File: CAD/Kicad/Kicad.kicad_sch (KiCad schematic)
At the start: 0 parts

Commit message: Started KiCAD work
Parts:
- added C1, C2: C, symbol Device:C
- added J1: USB_B_Mini, symbol Connector:USB_B_Mini
- added R1: 150R, symbol Device:R
- added R2: 240R, symbol Device:R
- added U1: AMS1117, Package_TO_SOT_SMD:SOT-223-3_TabPin2, symbol Regulator_Linear:AMS1117
- added U2: ESP8266EX, Package_DFN_QFN:QFN-32-1EP_5x5mm_P0.5mm_EP3.45x3.45mm, symbol MCU_Espressif:ESP8266EX
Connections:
- new net: C2.2, U2.1 (VDDA)
- new net: J1.5 (GND), R2.2, U2.33 (GND)
- new net: R1.2, R2.1, U1.1 (ADJ)
- new net: C2.1, R1.1, U1.2 (VO)
- new net: C1.1, U1.3 (VI)
- new net: C1.2, J1.1 (VBUS)
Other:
- note added: "USB Interface"

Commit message: More PCB stuff
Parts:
- added R_USB_D+, R_USB_D-: 27R, symbol Device:R
- added SW1: SW_SPST, symbol Switch:SW_SPST
- added U3: FT230XS, Package_SO:SSOP-16_3.9x4.9mm_P0.635mm, symbol Interface_USB:FT230XS
- C1, C2: value C -> 10C
- renumbered R2 to R_CNTRL_1, R1 to R_CNTRL_2
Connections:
- net at U2.25 (U0RXD): now also U3.1 (TXD)
- net at U2.26 (U0TXD): now also U3.4 (RXD)
- net GND: now reaches J1.5 (GND), R_CNTRL_1.2, U2.33 (GND)
- net GND: now also J1.SH (Shield), SW1.2 (B)
- net VCC: now reaches C2.1, R_CNTRL_2.1, U1.2 (VO)
- net VCC: now also U3.3 (VCCIO)
- net +5V: now reaches C1.2, J1.1 (VBUS)
- net at J1.2 (D-): now also R_USB_D-.1
- net at J1.3 (D+): now also R_USB_D+.2
- net at J1.4 (ID): now also SW1.1 (A)
- new net: R_USB_D-.2, U3.9 (USBDM)
- new net: U3.13 (GND), U3.5 (GND)
- new net: R_USB_D+.1, U3.8 (USBDP)
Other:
- note added: "Switch to change USB operation mode"
- moved on the sheet: C1, J1

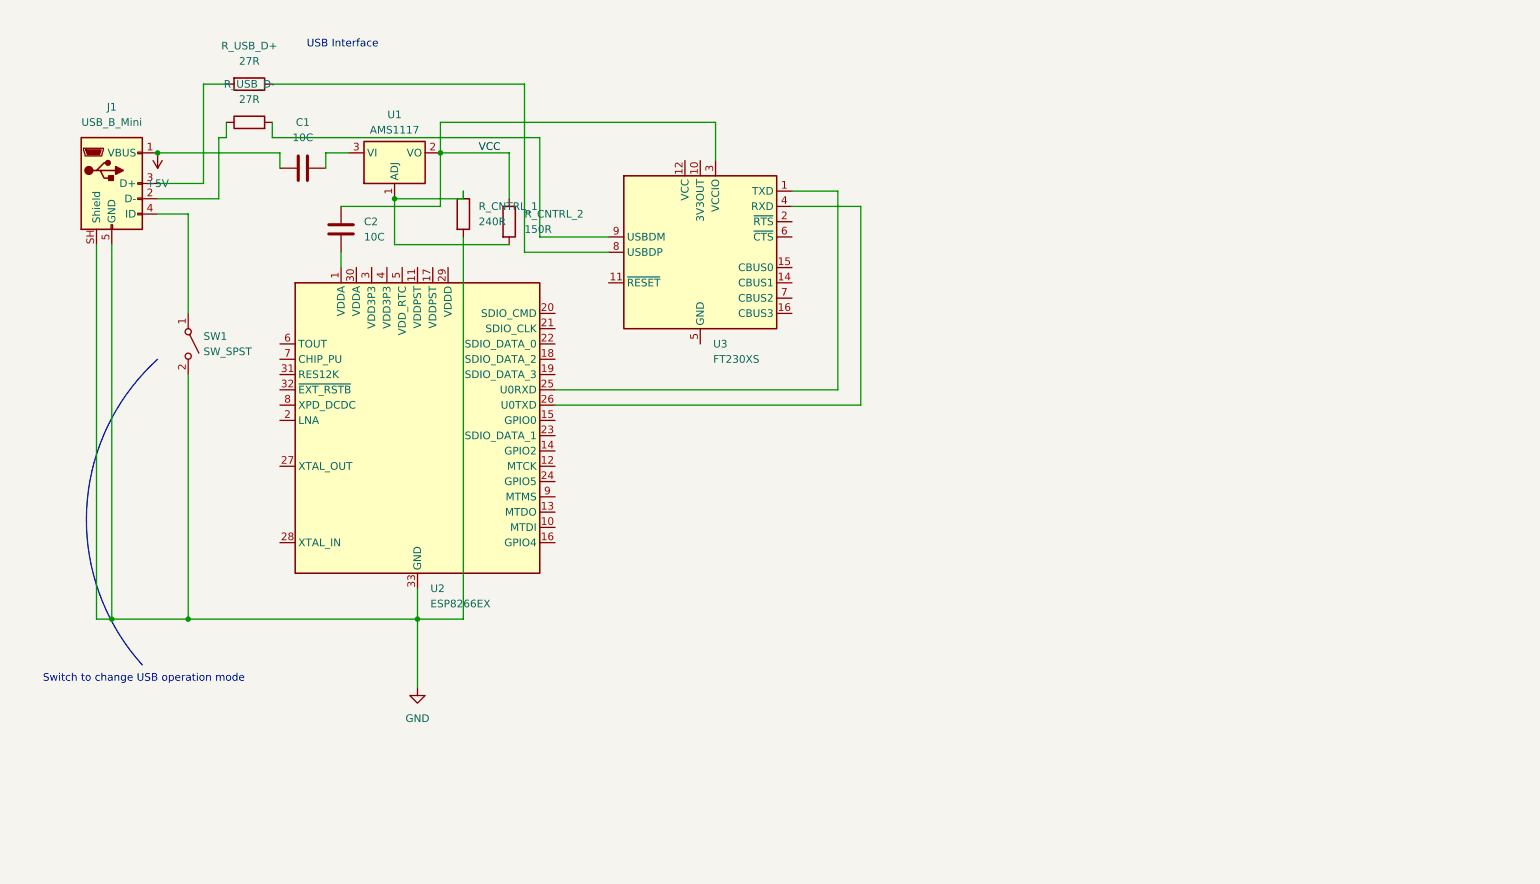
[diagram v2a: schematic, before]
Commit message: Added more and finalize basic serial connection
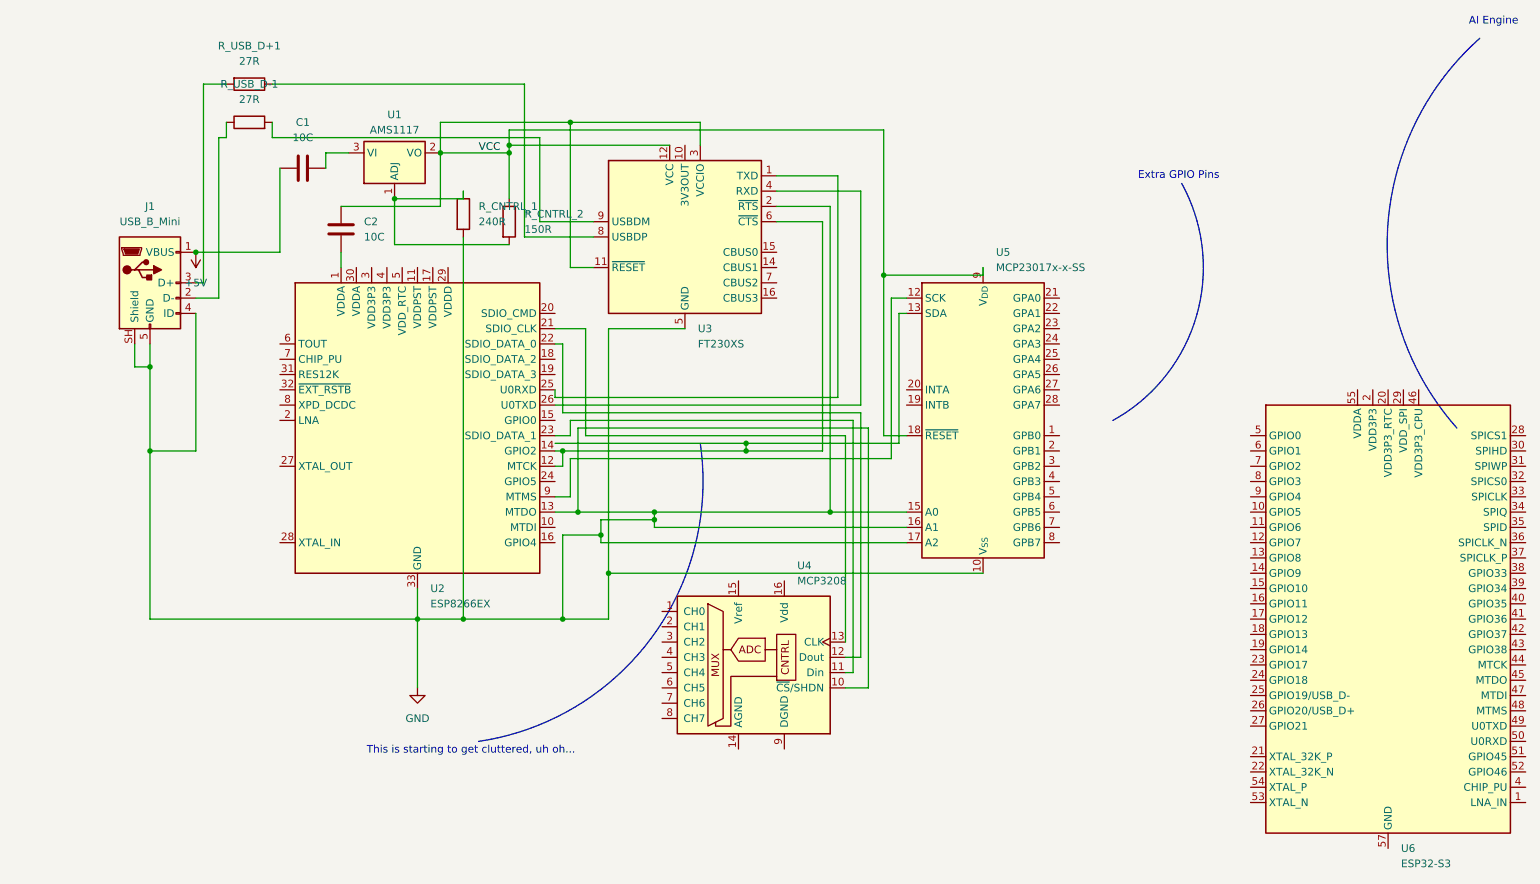
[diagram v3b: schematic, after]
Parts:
- removed SW1: SW_SPST, symbol Switch:SW_SPST
- added U4: MCP3208, symbol Analog_ADC:MCP3208
- added U5: MCP23017x-x-SS, Package_SO:SSOP-28_5.3x10.2mm_P0.65mm, symbol Interface_Expansion:MCP23017x-x-SS
- added U6: ESP32-S3, Package_DFN_QFN:QFN-56-1EP_7x7mm_P0.4mm_EP4x4mm, symbol MCU_Espressif:ESP32-S3
- renumbered R_USB_D+ to R_USB_D+1, R_USB_D- to R_USB_D-1
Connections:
- net GND: now also J1.4 (ID), U2.13 (MTDO), U3.13 (GND), U3.2 (~{RTS}), U3.5 (GND), U4.10 (~{CS}/SHDN), U5.10 (V_{SS}), U5.15 (A0), U5.16 (A1), U5.17 (A2)
- net VCC: now also U3.11 (~{RESET}), U3.12 (VCC), U5.18 (~{RESET}), U5.9 (V_{DD})
- net at U2.12 (MTCK): now also U2.14 (GPIO2), U3.6 (~{CTS}), U5.13 (SDA)
- net at U2.21 (SDIO_CLK): now also U4.13 (CLK)
- net at U2.22 (SDIO_DATA_0): now also U4.12 (Dout)
- net at U2.23 (SDIO_DATA_1): now also U4.11 (Din)
- net at U2.9 (MTMS): now also U5.12 (SCK)
- new net: U6.2 (VDD3P3), U6.3 (VDD3P3)
- new net: U6.55 (VDDA), U6.56 (VDDA)
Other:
- note added: "AI Engine"
- note added: "Extra GPIO Pins"
- note added: "This is starting to get cluttered, uh oh..."
- note removed: "Switch to change USB operation mode"
- note removed: "USB Interface"
- moved on the sheet: J1, U3

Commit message: Tweaked out and redid the entire main PCB on a Tuesday Afternoon
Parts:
- removed J1: USB_B_Mini, symbol Connector:USB_B_Mini
- removed R_CNTRL_1: 240R, symbol Device:R
- removed R_CNTRL_2: 150R, symbol Device:R
- removed R_USB_D+1, R_USB_D-1: 27R, symbol Device:R
- removed U1: AMS1117, Package_TO_SOT_SMD:SOT-223-3_TabPin2, symbol Regulator_Linear:AMS1117
- removed U2: ESP8266EX, Package_DFN_QFN:QFN-32-1EP_5x5mm_P0.5mm_EP3.45x3.45mm, symbol MCU_Espressif:ESP8266EX
- removed U3: FT230XS, Package_SO:SSOP-16_3.9x4.9mm_P0.635mm, symbol Interface_USB:FT230XS
- removed U4: MCP3208, symbol Analog_ADC:MCP3208
- removed U5: MCP23017x-x-SS, Package_SO:SSOP-28_5.3x10.2mm_P0.65mm, symbol Interface_Expansion:MCP23017x-x-SS
- removed U6: ESP32-S3, Package_DFN_QFN:QFN-56-1EP_7x7mm_P0.4mm_EP4x4mm, symbol MCU_Espressif:ESP32-S3
- added AE1: PCB_ANT, symbol Device:Antenna_Dipole
- added C10: 100nF, symbol Device:C
- added C3, C4: 0.1uF, symbol Device:C
- added C5: 1uF, symbol Device:C
- added C6, C7, C8, C9: C, symbol Device:C
- added D1, D2: LED, symbol Device:LED
- added D3: PWR_LED_1, symbol Device:LED
- added D4: PWR_LED_2, symbol Device:LED
- added FB1: FerriteBead, symbol Device:FerriteBead
- added J1: USB_C_Receptacle_USB2.0_14P, symbol Connector:USB_C_Receptacle_USB2.0_14P
- added J2: PWR_CONN, symbol Connector:Conn_01x03_Pin
- added L1: L, symbol Device:L
- added L2: 4.3nH, symbol Device:L
- added R1, R2: R, symbol Device:R
- added R_PWR_ADJ_1: 60, symbol Device:R
- added R_PWR_ADJ_2: 100, symbol Device:R
- added R_SPI_CLOCK: 200, symbol Device:R
- added U1: ESP8266EX, Package_DFN_QFN:QFN-32-1EP_5x5mm_P0.5mm_EP3.45x3.45mm, symbol MCU_Espressif:ESP8266EX
- added U2: AMS1117, Package_TO_SOT_SMD:SOT-223-3_TabPin2, symbol Regulator_Linear:AMS1117
- added U3: SST25VF080B-50-4x-S2Ax, Package_SO:SOIC-8_5.3x5.3mm_P1.27mm, symbol Memory_Flash:SST25VF080B-50-4x-S2Ax
- added U4: FT230XS, Package_SO:SSOP-16_3.9x4.9mm_P0.635mm, symbol Interface_USB:FT230XS
- added U5: ESP32-S3, Package_DFN_QFN:QFN-56-1EP_7x7mm_P0.4mm_EP4x4mm, symbol MCU_Espressif:ESP32-S3
- added Y1: Crystal_GND24, symbol Device:Crystal_GND24
- C1, C2: value 10C -> C
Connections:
- net GND: now also C1.1, C2.1, AE1.1, C3.1, C4.1, C5.1, C6.1, C7.1, C8.2, C9.2, FB1.2, J2.3 (Pin_3), L2.1, R1.2, R_PWR_ADJ_2.2, U1.3 (VDD3P3), U1.33 (GND), U1.4 (VDD3P3), U3.4 (VSS), U4.13 (GND), U4.5 (GND), Y1.2 (G), Y1.4 (G)
- net VCC: now also C10.1, C3.2, C4.2, C5.2, C6.2, L2.2, R_PWR_ADJ_1.1, U1.1 (VDDA), U1.29 (VDDD), U1.30 (VDDA), U2.2 (VO), U3.8 (VDD); no longer C2.1
- net at C2.2: now also AE1.2, L1.1
- net +5V: no longer names the net of C1.2
- net +5V: now also L1.2, U1.2 (LNA)
- new net: FB1.1, J1.A1 (GND), J1.A12 (GND), J1.B1 (GND), J1.B12 (GND), J1.SH (SHIELD)
- new net: U4.10 (3V3OUT), U4.3 (VCCIO)
- new net: C10.2, D1.2 (A), D2.2 (A), U4.12 (VCC)
- new net: D2.1 (K), U4.14 (CBUS1)
- new net: D1.1 (K), U4.7 (CBUS2)
- new net: C7.2, R2.1, Y1.1
- new net: R_SPI_CLOCK.1, U1.21 (SDIO_CLK)
- new net: R_SPI_CLOCK.2, U3.6 (SCK)
- new net: U1.18 (SDIO_DATA_2), U3.7 (~{HOLD})
- new net: U1.19 (SDIO_DATA_3), U3.3 (~{WP})
- new net: U1.20 (SDIO_CMD), U3.1 (~{CE})
- new net: U1.22 (SDIO_DATA_0), U3.2 (SO)
- new net: U1.23 (SDIO_DATA_1), U3.5 (SI)
- new net: R1.1, U1.31 (RES12K)
- new net: U5.2 (VDD3P3), U5.3 (VDD3P3)
- new net: U5.55 (VDDA), U5.56 (VDDA)
- new net: R_PWR_ADJ_1.2, R_PWR_ADJ_2.1, U2.1 (ADJ)
- new net 5V: C9.1, D3.1 (K), D3.2 (A), D4.1 (K), D4.2 (A), J1.A4 (VBUS), J1.A9 (VBUS), J1.B4 (VBUS), J1.B9 (VBUS), J2.1 (Pin_1), J2.2 (Pin_2), U2.3 (VI)
- new net ESP_8266_USB_D+: J1.A6 (D+), J1.B6 (D+), U4.8 (USBDP)
- new net ESP_8266_USB_D-: J1.A7 (D-), J1.B7 (D-), U4.9 (USBDM)
- new net ESP_8266_XIN: R2.2
- new net ESP_8266_XOUT: C8.1, Y1.3
- new net XIN: U1.27 (XTAL_OUT)
- new net XOUT: U1.28 (XTAL_IN)
- new net ZIRU_U0RXD: U1.25 (U0RXD)
- new net ZRIU_U0TXD: U1.26 (U0TXD)
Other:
- note added: "Basic Power Supply"
- note added: "Crystal Circuit To Drive ZRIU"
- note added: "ESP8266 Zero Ring Interface Unit (ZRI)"
- note added: "Flash"
- note added: "USB to UART IC"
- note added: "Values of L1, C1, and C2 are soon to be found"
- note added: "ZRIU USB Port"
- note removed: "AI Engine"
- note removed: "Extra GPIO Pins"
- note removed: "This is starting to get cluttered, uh oh..."
- title: (none) -> Cloudboard Processing Main Unit

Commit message: Fixed and added journal entries
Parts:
- added AE2: PCB_ANT, symbol Device:Antenna_Dipole
- added C11, C12, C13, C14: C, symbol Device:C
- added D5: SD05C-01F, Diode_SMD:D_SOD-323, symbol Diode:SD05C-01F
- added L3, L4: L, symbol Device:L
- C6: value C -> 1uF
- R12K: renamed from R1; value R -> 12K
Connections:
- net GND: now also U5.57 (GND), AE2.1, C11.2, C12.2, C13.2, C14.2, D5.1 (A1)
- net at U5.1 (LNA_IN): now also C11.1, L3.1
- new net: AE2.2, C14.1, D5.2 (A2), L4.2
- new net: C12.1, C13.1, L3.2, L4.1
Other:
- note added: "(Matching of Antenna)"
- note added: "(Matching of Chip)"
- note added: "All varibles past LNA_IN are TBD"
- note added: "Missing values are soon to be found"
- note added: "Single-ended 50 ohm RF traces"
- moved on the sheet: R12K, U5

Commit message: It's super late man
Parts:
- removed U5: ESP32-S3, Package_DFN_QFN:QFN-56-1EP_7x7mm_P0.4mm_EP4x4mm, symbol MCU_Espressif:ESP32-S3
- added C15, C16: 0.1uF, symbol Device:C
- added C17, C20: 1uF, symbol Device:C
- added C18: 10uF, symbol Device:C
- added C19: 10nF, symbol Device:C
- added C21, C22, C24: C, symbol Device:C
- added C23: 100nF, symbol Device:C
- added D6, D7: LED, symbol Device:LED
- added FB2, FB3: FerriteBead, symbol Device:FerriteBead
- added J3: RJ12_Shielded, symbol Connector:RJ12_Shielded
- added J4, J5: USB_C_Receptacle_USB2.0_14P, symbol Connector:USB_C_Receptacle_USB2.0_14P
- added J6: Conn_01x24_Pin, symbol Connector:Conn_01x24_Pin
- added L5: 2.0nH, symbol Device:L
- added L6: L, symbol Device:L
- added R1: 499, symbol Device:R
- added R_PWR_ADJ_3: 60, symbol Device:R
- added R_PWR_ADJ_4: 100, symbol Device:R
- added U5: ESP32-S3-NEW, Package_DFN_QFN:QFN-56-1EP_7x7mm_P0.4mm_EP4x4mm, symbol New_Library:ESP32-S3-NEW
- added U6: FT230XS, Package_SO:SSOP-16_3.9x4.9mm_P0.635mm, symbol Interface_USB:FT230XS
- added U7: AMS1117, Package_TO_SOT_SMD:SOT-223-3_TabPin2, symbol Regulator_Linear:AMS1117
- added U8: SST25VF080B-50-4x-S2Ax, Package_SO:SOIC-8_5.3x5.3mm_P1.27mm, symbol Memory_Flash:SST25VF080B-50-4x-S2Ax
- added Y2: Crystal_GND23, symbol Device:Crystal_GND23
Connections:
- net ZIRU_U0RXD is gone; now on net ZRI_U0RXD: U1.25 (U0RXD)
- net ZRIU_U0TXD is gone; now on net ZRI_U0TXD: U1.26 (U0TXD)
- net GND: now also C15.2, C16.2, C17.2, C18.2, C19.2, C20.2, C21.1, C22.1, C24.2, FB2.2, FB3.2, J3.1, J3.SH, R_PWR_ADJ_4.2, U5.57 (GND), U6.13 (GND), U6.5 (GND), U8.4 (VSS), Y2.2 (G), Y2.3 (G)
- net at C11.1, L3.1: now also U5.1 (LNA_IN)
- net ZRI_U0RXD: now reaches U4.1 (TXD)
- net ZRI_U0TXD: now reaches C10.2, D1.2 (A), D2.2 (A), U4.12 (VCC)
- net ZRI_U0TXD: now also U4.4 (RXD)
- net 5V renamed A_5V
- net A_5V: no longer D4.1 (K), D4.2 (A), J2.2 (Pin_2)
- net VCC renamed VCC0
- net VCC0: now also C23.1, R_PWR_ADJ_3.1, U7.2 (VO), U8.8 (VDD)
- new net: C21.2, L6.1, Y2.1
- new net: D6.1 (K), U6.7 (CBUS2)
- new net: FB3.1, J5.A1 (GND), J5.A12 (GND), J5.B1 (GND), J5.B12 (GND), J5.SH (SHIELD)
- new net: D7.1 (K), U6.14 (CBUS1)
- new net: C15.1, L5.2, U5.2 (VDD3P3), U5.3 (VDD3P3), U5.56 (VDDA)
- new net: J5.A6 (D+), J5.B6 (D+), U5.26 (GPIO20/USB_D+)
- new net: J5.A7 (D-), J5.B7 (D-), U5.25 (GPIO19/USB_D-)
- new net: FB2.1, J4.A1 (GND), J4.A12 (GND), J4.B1 (GND), J4.B12 (GND), J4.SH (SHIELD)
- new net: R_PWR_ADJ_3.2, R_PWR_ADJ_4.1, U7.1 (ADJ)
- new net: U5.32 (SPICS0), U8.1 (~{CE})
- new net: U5.34 (SPIQ), U8.2 (SO)
- new net: U5.31 (SPIWP), U8.3 (~{WP})
- new net: U5.35 (SPID), U8.5 (SI)
- new net: U5.33 (SPICLK), U8.6 (SCK)
- new net: U5.30 (SPIHD), U8.7 (~{HOLD})
- new net: U6.10 (3V3OUT), U6.3 (VCCIO)
- new net: J3.6, U5.13 (GPIO8)
- new net: J3.5, U5.14 (GPIO9)
- new net: R1.1, U5.49 (U0TXD)
- new net B_5V: C24.1, D4.1 (K), D4.2 (A), J2.2 (Pin_2), J4.A4 (VBUS), J4.A9 (VBUS), J4.B4 (VBUS), J4.B9 (VBUS), J5.A4 (VBUS), J5.A9 (VBUS), J5.B4 (VBUS), J5.B9 (VBUS), U7.3 (VI)
- new net MPU_U0RXD: U5.50 (U0RXD), U6.1 (TXD)
- new net MPU_U0TXD: C23.2, D6.2 (A), D7.2 (A), R1.2, U6.12 (VCC), U6.4 (RXD)
- new net MPU_UART_USB_D+: J4.A6 (D+), J4.B6 (D+), U6.8 (USBDP)
- new net MPU_UART_USB_D-: J4.A7 (D-), J4.B7 (D-), U6.9 (USBDM)
- new net VCC1: C16.1, C17.1, C18.1, C19.1, C20.1, J3.4, L5.1, U5.55 (VDDA), U5.56 (VDDA)
- new net XTAL_N: C22.2, U5.53 (XTAL_N), Y2.4
- new net XTAL_P: L6.2, U5.54 (XTAL_P)
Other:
- note added: "40 MhZ +- 10PPM"
- note added: "40MhZ +- 10 PPM"
- note added: "Crystal Circuit To Drive ZRI"
- note added: "Crystal Unit for ESP32-S3"
- note added: "Database and hub connections will be initialized through I2C VIA GPIO pins 8 carrying data and 9 carrying clock"
- note added: "ESP-S3 ANT"
- note added: "MPU Direct USB Port"
- note added: "MPU Power Supply"
- note added: "MPU UART USB Port"
- note added: "MPU USB to UART IC"
- note added: "Soon to be GPIO headers"
- note added: "ZRI Flash"
- note added: "ZRI Power Supply"
- note added: "ZRI USB Port"
- note removed: "Basic Power Supply"
- note removed: "Crystal Circuit To Drive ZRIU"
- note removed: "Flash"
- note removed: "ZRIU USB Port"
- moved on the sheet: AE2, C11, C12, C13, C14, D3, D4, D5, J2, L3, L4

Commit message: revised sensor board and redid I2C connections to both MCUs
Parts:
- removed J2: PWR_CONN, symbol Connector:Conn_01x03_Pin
- added C25: C, symbol Device:C
- added D8: PWR_LED_3, symbol Device:LED
- added J2: Conn_01x04_Pin, symbol Connector:Conn_01x04_Pin
- added R3: 27K, symbol Device:R
- added R_PWR_ADJ_5: 60, symbol Device:R
- added R_PWR_ADJ_6: 100, symbol Device:R
- added U9: AMS1117, Package_TO_SOT_SMD:SOT-223-3_TabPin2, symbol Regulator_Linear:AMS1117
- C21, C22, C7, C8: value C -> 20pF
- R2: value R -> 27K
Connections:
- net A_5V: now also J2.1 (Pin_1)
- net B_5V: now also C25.1, J2.2 (Pin_2), U9.3 (VI)
- net ESP_8266_XIN: now also C7.2, Y1.1; no longer R2.2
- net GND: now also C25.2, J2.4 (Pin_4), R_PWR_ADJ_6.2
- net VCC1: no longer J3.4
- net MAIN_BUS_I2C_SCK: now reaches U1.14 (GPIO2)
- net MAIN_BUS_I2C_SCK: now also J3.5, R3.1
- net MAIN_BUS_I2C_SDA: now reaches U1.9 (MTMS)
- net MAIN_BUS_I2C_SDA: now also J3.6, R2.1
- net at U5.13 (GPIO8): now also R2.2; no longer J3.6
- net at U5.14 (GPIO9): now also R3.2; no longer J3.5
- net C_5V: now reaches J3.3
- net C_5V: now also D8.1 (K), D8.2 (A), J2.3 (Pin_3)
- new net: R_PWR_ADJ_5.2, R_PWR_ADJ_6.1, U9.1 (ADJ)
- new net VCC2: J3.4, R_PWR_ADJ_5.1, U9.2 (VO)
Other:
- note added: "Add R1 if needed"
- note added: "External plugs to power both MCU units and sensing board [5V ONLY!!!]"
- note added: "I2C Pull up"
- note added: "I2C Serial connection to join both MCUs"
- note added: "Maybe find a better way to carry I2C..."
- note added: "RJ12 sensor board connector"
- note added: "Sensor 3v3 supply"
- note added: "Values subject to change"
- note removed: "Missing values are soon to be found"
- moved on the sheet: C21, C22, D3, D4, J6, L6, Y2
